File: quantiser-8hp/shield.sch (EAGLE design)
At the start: 27 parts

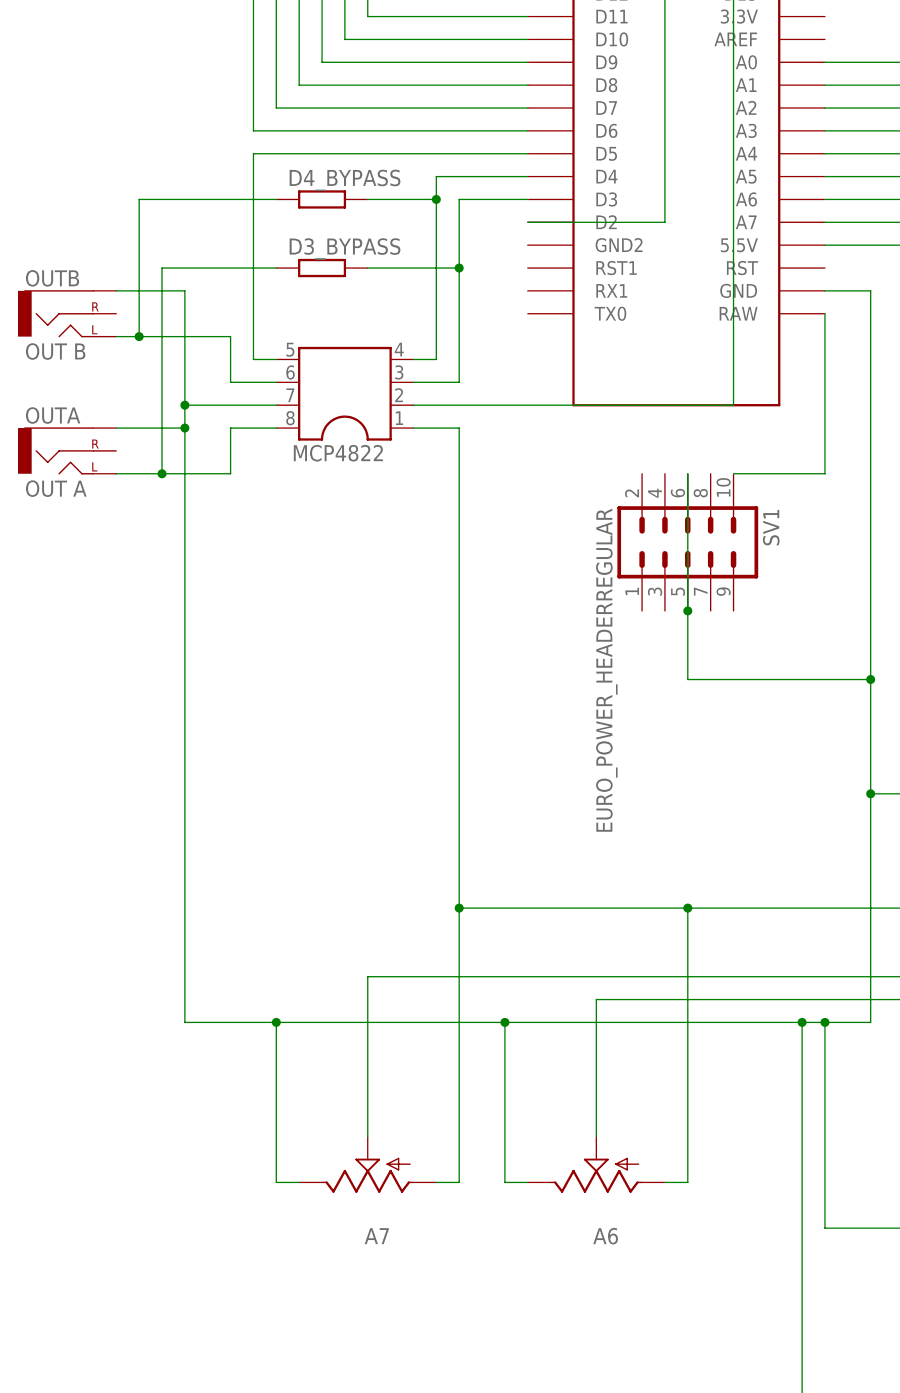
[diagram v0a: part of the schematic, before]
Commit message: Replace 12hp quantiser with 8hp version
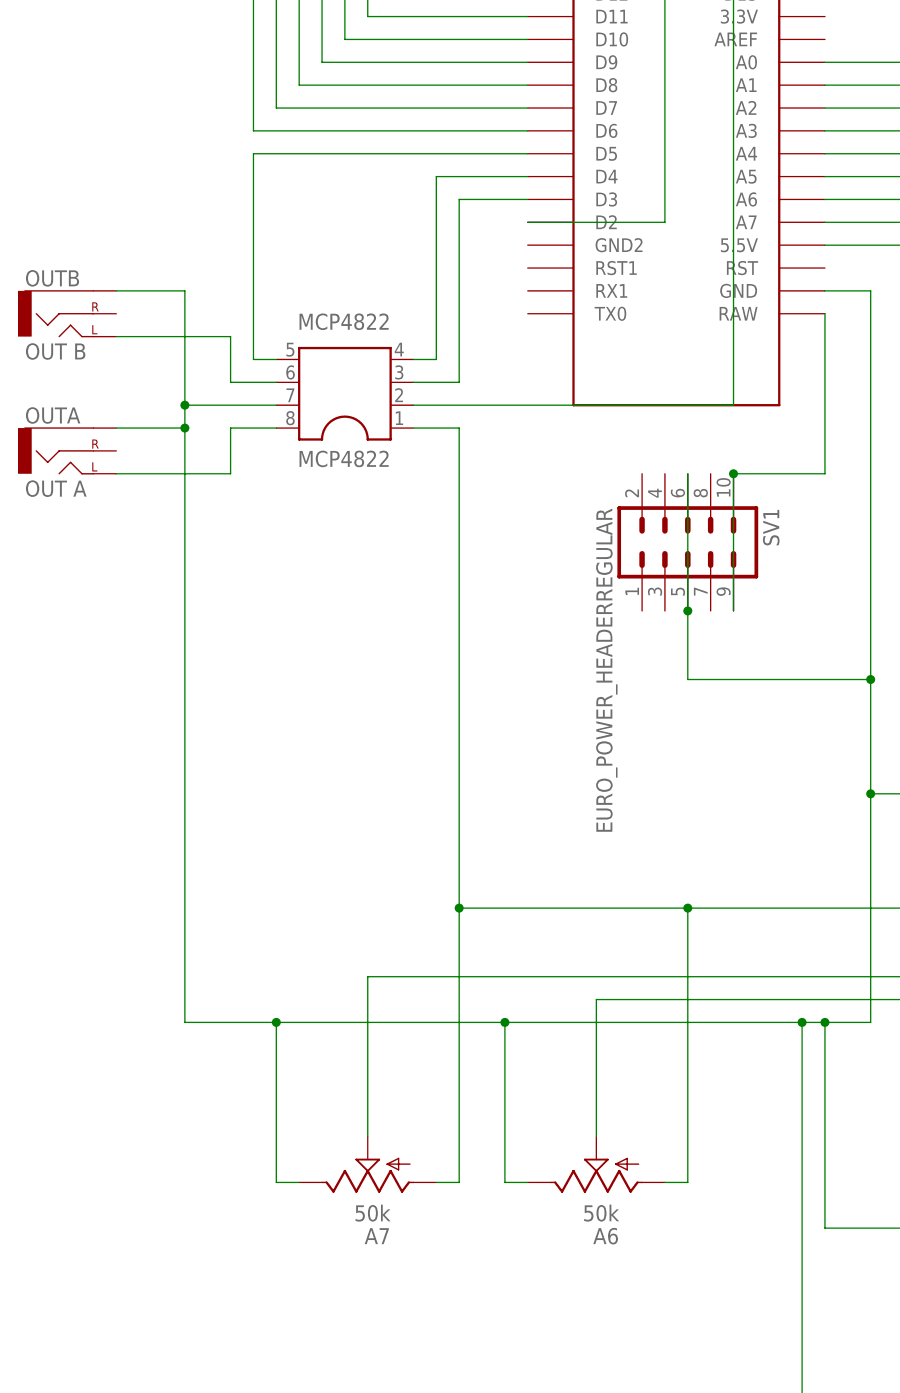
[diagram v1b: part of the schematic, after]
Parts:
- removed D3_BYPASS, D4_BYPASS: (no value), MusicThingModular:RESISTOR7MM
- A6, A7: value (none) -> 50k
- MCP4822: value (none) -> MCP4822
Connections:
- net N$1: now also SV1.9
- net N$17: no longer D3_BYPASS.1
- net N$18: no longer D4_BYPASS.1
- net N$20: no longer D3_BYPASS.2
- net N$21: no longer D4_BYPASS.2
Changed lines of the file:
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@@
 <part name="U$1" library="Arduino-clone" deviceset="NANO" device=""/>
 <part name="SV1" library="MusicThingModular" deviceset="EURO_POWER_HEADER" device="REGULAR"/>
-<part name="MCP4822" library="ic-package" library_urn="urn:adsk.eagle:library:239" deviceset="DIL8" device="" package3d_urn="urn:adsk.eagle:package:29519/2"/>
+<part name="MCP4822" library="ic-package" library_urn="urn:adsk.eagle:library:239" deviceset="DIL8" device="" package3d_urn="urn:adsk.eagle:package:29519/2" value="MCP4822"/>
 <part name="OUTA" library="MusicThingModular" deviceset="THONKI-STEREO" device="" value="OUT A"/>
 <part name="OUTB" library="MusicThingModular" deviceset="THONKI-STEREO" device="" value="OUT B"/>
 <part name="A4" library="MusicThingModular" deviceset="THONKI-STEREO" device=""/>
 <part name="A5" library="MusicThingModular" deviceset="THONKI-STEREO" device=""/>
-<part name="A7" library="MusicThingModular" deviceset="9MM_SNAP-IN_POT" device="_"/>
-<part name="A6" library="MusicThingModular" deviceset="9MM_SNAP-IN_POT" device="_"/>
+<part name="A7" library="MusicThingModular" deviceset="9MM_SNAP-IN_POT" device="_" value="50k"/>
+<part name="A6" library="MusicThingModular" deviceset="9MM_SNAP-IN_POT" device="_" value="50k"/>
 <part name="R13" library="SparkFun-Resistors" library_urn="urn:adsk.eagle:library:532" deviceset="10KOHM" device="-HORIZ-1/4W-5%" package3d_urn="urn:adsk.eagle:package:39658/1" value="220k"/>
 <part name="R14" library="SparkFun-Resistors" library_urn="urn:adsk.eagle:library:532" deviceset="10KOHM" device="-HORIZ-1/4W-5%" package3d_urn="urn:adsk.eagle:package:39658/1" value="220k"/>
 <part name="R15" library="SparkFun-Resistors" library_urn="urn:adsk.eagle:library:532" deviceset="10KOHM" device="-HORIZ-1/4W-5%" package3d_urn="urn:adsk.eagle:package:39658/1" value="150k"/>
 <part name="R16" library="SparkFun-Resistors" library_urn="urn:adsk.eagle:library:532" deviceset="10KOHM" device="-HORIZ-1/4W-5%" package3d_urn="urn:adsk.eagle:package:39658/1" value="150k"/>
-<part name="D3_BYPASS" library="MusicThingModular" deviceset="RESISTOR" device="7MM"/>
-<part name="D4_BYPASS" library="MusicThingModular" deviceset="RESISTOR" device="7MM"/>
 </parts>
 <sheets>
@@
 </instance>
 <instance part="MCP4822" gate="G$1" x="-71.12" y="-25.4" smashed="yes" rot="R180">
-<attribute name="NAME" x="-66.675" y="-29.845" size="1.778" layer="95" rot="R180"/>
-<attribute name="VALUE" x="-66.675" y="-16.51" size="1.778" layer="96" rot="R180"/>
+<attribute name="NAME" x="-66.04" y="-30.48" size="1.778" layer="95" rot="R180"/>
+<attribute name="VALUE" x="-66.04" y="-15.24" size="1.778" layer="96" rot="R180"/>
 </instance>
 <instance part="OUTA" gate="G$1" x="-101.6" y="-30.48" smashed="yes">
@@
 <attribute name="NAME" x="18.796" y="-111.76" size="1.778" layer="95" font="vector" rot="R90" align="bottom-center"/>
 <attribute name="VALUE" x="21.844" y="-111.76" size="1.778" layer="96" font="vector" rot="R90" align="top-center"/>
-</instance>
-<instance part="D3_BYPASS" gate="G$1" x="-73.66" y="-10.16" smashed="yes">
-<attribute name="NAME" x="-77.47" y="-8.6614" size="1.778" layer="95"/>
-<attribute name="VALUE" x="-77.47" y="-13.462" size="1.778" layer="96"/>
-</instance>
-<instance part="D4_BYPASS" gate="G$1" x="-73.66" y="-2.54" smashed="yes">
-<attribute name="NAME" x="-77.47" y="-1.0414" size="1.778" layer="95"/>
-<attribute name="VALUE" x="-77.47" y="-5.842" size="1.778" layer="96"/>
 </instance>
 </instances>
@@
 <wire x1="-17.78" y1="-15.24" x2="-17.78" y2="-33.02" width="0.1524" layer="91"/>
 <wire x1="-17.78" y1="-33.02" x2="-27.94" y2="-33.02" width="0.1524" layer="91"/>
+<pinref part="SV1" gate="G$1" pin="9"/>
+<wire x1="-27.94" y1="-33.02" x2="-27.94" y2="-48.26" width="0.1524" layer="91"/>
+<junction x="-27.94" y="-33.02"/>
 </segment>
 </net>
@@
 <wire x1="-78.74" y1="-22.86" x2="-83.82" y2="-22.86" width="0.1524" layer="91"/>
 <wire x1="-83.82" y1="-22.86" x2="-83.82" y2="-17.78" width="0.1524" layer="91"/>
-<wire x1="-83.82" y1="-17.78" x2="-93.98" y2="-17.78" width="0.1524" layer="91"/>
-<wire x1="-93.98" y1="-17.78" x2="-96.52" y2="-17.78" width="0.1524" layer="91"/>
-<wire x1="-78.74" y1="-2.54" x2="-93.98" y2="-2.54" width="0.1524" layer="91"/>
-<wire x1="-93.98" y1="-2.54" x2="-93.98" y2="-17.78" width="0.1524" layer="91"/>
-<junction x="-93.98" y="-17.78"/>
-<pinref part="D4_BYPASS" gate="G$1" pin="1"/>
+<wire x1="-83.82" y1="-17.78" x2="-96.52" y2="-17.78" width="0.1524" layer="91"/>
 </segment>
 </net>
@@
 <wire x1="-83.82" y1="-27.94" x2="-83.82" y2="-33.02" width="0.1524" layer="91"/>
 <pinref part="OUTA" gate="G$1" pin="LEFT"/>
-<wire x1="-83.82" y1="-33.02" x2="-91.44" y2="-33.02" width="0.1524" layer="91"/>
-<wire x1="-91.44" y1="-33.02" x2="-96.52" y2="-33.02" width="0.1524" layer="91"/>
-<wire x1="-78.74" y1="-10.16" x2="-91.44" y2="-10.16" width="0.1524" layer="91"/>
-<wire x1="-91.44" y1="-10.16" x2="-91.44" y2="-33.02" width="0.1524" layer="91"/>
-<junction x="-91.44" y="-33.02"/>
-<pinref part="D3_BYPASS" gate="G$1" pin="1"/>
+<wire x1="-83.82" y1="-33.02" x2="-96.52" y2="-33.02" width="0.1524" layer="91"/>
 </segment>
 </net>
@@
 <pinref part="MCP4822" gate="G$1" pin="3"/>
 <wire x1="-63.5" y1="-22.86" x2="-58.42" y2="-22.86" width="0.1524" layer="91"/>
-<wire x1="-58.42" y1="-22.86" x2="-58.42" y2="-10.16" width="0.1524" layer="91"/>
+<wire x1="-58.42" y1="-22.86" x2="-58.42" y2="-2.54" width="0.1524" layer="91"/>
 <pinref part="U$1" gate="G$1" pin="D3"/>
-<wire x1="-58.42" y1="-10.16" x2="-58.42" y2="-2.54" width="0.1524" layer="91"/>
 <wire x1="-58.42" y1="-2.54" x2="-50.8" y2="-2.54" width="0.1524" layer="91"/>
-<wire x1="-68.58" y1="-10.16" x2="-58.42" y2="-10.16" width="0.1524" layer="91"/>
-<junction x="-58.42" y="-10.16"/>
-<pinref part="D3_BYPASS" gate="G$1" pin="2"/>
 </segment>
 </net>
@@
 <pinref part="MCP4822" gate="G$1" pin="4"/>
 <wire x1="-63.5" y1="-20.32" x2="-60.96" y2="-20.32" width="0.1524" layer="91"/>
-<wire x1="-60.96" y1="-20.32" x2="-60.96" y2="-2.54" width="0.1524" layer="91"/>
+<wire x1="-60.96" y1="-20.32" x2="-60.96" y2="0" width="0.1524" layer="91"/>
 <pinref part="U$1" gate="G$1" pin="D4"/>
-<wire x1="-60.96" y1="-2.54" x2="-60.96" y2="0" width="0.1524" layer="91"/>
 <wire x1="-60.96" y1="0" x2="-50.8" y2="0" width="0.1524" layer="91"/>
-<wire x1="-68.58" y1="-2.54" x2="-60.96" y2="-2.54" width="0.1524" layer="91"/>
-<junction x="-60.96" y="-2.54"/>
-<pinref part="D4_BYPASS" gate="G$1" pin="2"/>
-</segment>
-</net>
+</segment>
+</net>
